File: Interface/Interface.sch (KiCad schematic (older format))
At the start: 5 parts, among them U1 PC123

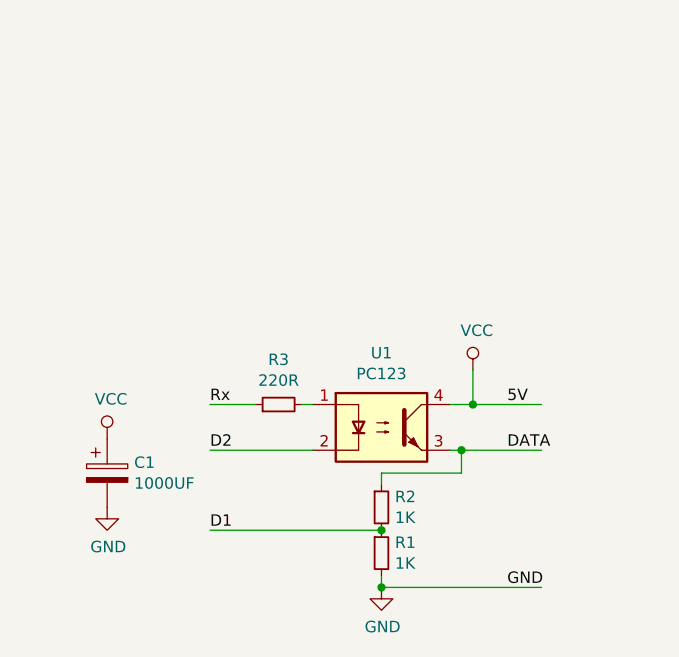
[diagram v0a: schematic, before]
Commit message: Updated interface schematic
Updated interface schematic, now using 1 bit bus transceiver
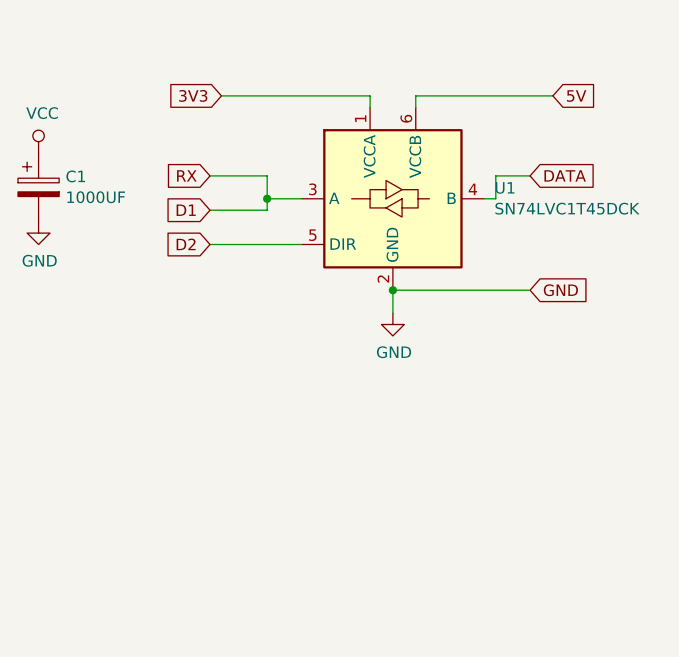
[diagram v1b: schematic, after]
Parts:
- removed R1, R2: 1K, symbol Device:R_Small
- removed R3: 220R, symbol Device:R_Small
- removed U1: PC123, Package_DIP:DIP-4_W7.62mm, symbol Isolator:PC817
- added U1: SN74LVC1T45DCK, Package_TO_SOT_SMD:SOT-363_SC-70-6, symbol Logic_LevelTranslator:SN74LVC1T45DCK
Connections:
- net labels added: 3V3, RX
- net labels removed: Rx
- wire segments 14 -> 15
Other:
- moved on the sheet: C1
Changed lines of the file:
@@
 EESchema Schematic File Version 4
+LIBS:Interface-cache
 EELAYER 30 0
 EELAYER END
@@
 $EndDescr
 $Comp
-L Isolator:PC817 U1
-U 1 1 5D6EC97C
-P 5150 2950
-F 0 "U1" H 5150 3275 50  0000 C CNN
-F 1 "PC123" H 5150 3184 50  0000 C CNN
-F 2 "Package_DIP:DIP-4_W7.62mm" H 4950 2750 50  0001 L CIN
-F 3 "http://www.soselectronic.cz/a_info/resource/d/pc817.pdf" H 5150 2950 50  0001 L CNN
-	1    5150 2950
+L power:VCC #PWR?
+U 1 1 5D70837B
+P 3650 1750
+F 0 "#PWR?" H 3650 1600 50  0001 C CNN
+F 1 "VCC" H 3667 1923 50  0000 C CNN
+F 2 "" H 3650 1750 50  0001 C CNN
+F 3 "" H 3650 1750 50  0001 C CNN
+	1    3650 1750
+	1    0    0    -1
+$EndComp
+$Comp
+L Logic_LevelTranslator:SN74LVC1T45DCK U1
+U 1 1 5E9CDB6D
+P 5200 1950
+F 0 "U1" H 5644 1996 50  0000 L CNN
+F 1 "SN74LVC1T45DCK" H 5644 1905 50  0000 L CNN
+F 2 "Package_TO_SOT_SMD:SOT-363_SC-70-6" H 5200 1500 50  0001 C CNN
+F 3 "http://www.ti.com/lit/ds/symlink/sn74lvc1t45.pdf" H 4300 1300 50  0001 C CNN
+	1    5200 1950
 	1    0    0    -1
 $EndComp
 Wire Wire Line
-	4800 2850 4850 2850
+	4400 2150 4800 2150
 Wire Wire Line
-	4600 2850 4400 2850
-Text Label 4400 2850 0    50   ~ 0
-Rx
+	5300 1550 5300 1500
 Wire Wire Line
-	4850 3050 4400 3050
-Text Label 4400 3050 0    50   ~ 0
+	5100 1550 5100 1500
+Text GLabel 4400 1850 0    50   Input ~ 0
+RX
+Text GLabel 4400 2000 0    50   Input ~ 0
+D1
+Text GLabel 5800 1850 2    50   Input ~ 0
+DATA
+Text GLabel 5800 2350 2    50   Input ~ 0
+GND
+Text GLabel 5900 1500 2    50   Input ~ 0
+5V
+Text GLabel 4450 1500 0    50   Input ~ 0
+3V3
+Text GLabel 4400 2150 0    50   Input ~ 0
 D2
+Wire Wire Line
+	4650 1850 4650 1950
+Wire Wire Line
+	4650 1950 4800 1950
+Wire Wire Line
+	4650 2000 4650 1950
+Wire Wire Line
+	4400 2000 4650 2000
+Connection ~ 4650 1950
+Wire Wire Line
+	4400 1850 4650 1850
+Wire Wire Line
+	5100 1500 4450 1500
+Wire Wire Line
+	5200 2350 5800 2350
+Wire Wire Line
+	5300 1500 5900 1500
+Wire Wire Line
+	5600 1950 5650 1950
+Wire Wire Line
+	5650 1950 5650 1850
+Wire Wire Line
+	5650 1850 5800 1850
 $Comp
-L power:VCC #PWR?
-U 1 1 5D6F0E03
-P 5550 2700
-F 0 "#PWR?" H 5550 2550 50  0001 C CNN
-F 1 "VCC" H 5567 2873 50  0000 C CNN
-F 2 "" H 5550 2700 50  0001 C CNN
-F 3 "" H 5550 2700 50  0001 C CNN
-	1    5550 2700
-	1    0    0    -1
-$EndComp
-Wire Wire Line
-	5450 3050 5500 3050
-Text Label 5700 3050 0    50   ~ 0
-DATA
-Text Label 4400 3400 0    50   ~ 0
-D1
-$Comp
-L power:GND #PWR?
-U 1 1 5D6F335B
-P 5150 3650
-F 0 "#PWR?" H 5150 3400 50  0001 C CNN
-F 1 "GND" H 5155 3477 50  0000 C CNN
-F 2 "" H 5150 3650 50  0001 C CNN
-F 3 "" H 5150 3650 50  0001 C CNN
-	1    5150 3650
-	1    0    0    -1
-$EndComp
-Wire Wire Line
-	5450 2850 5550 2850
-Wire Wire Line
-	5550 2700 5550 2850
-Connection ~ 5550 2850
-Wire Wire Line
-	5550 2850 5850 2850
-$Comp
-L Device:R_Small R2
-U 1 1 5D6F2079
-P 5150 3300
-F 0 "R2" H 5209 3346 50  0000 L CNN
-F 1 "1K" H 5209 3255 50  0000 L CNN
-F 2 "" H 5150 3300 50  0001 C CNN
-F 3 "~" H 5150 3300 50  0001 C CNN
-	1    5150 3300
-	1    0    0    -1
-$EndComp
-$Comp
-L Device:R_Small R3
-U 1 1 5D6EE00F
-P 4700 2850
-F 0 "R3" V 4896 2850 50  0000 C CNN
-F 1 "220R" V 4805 2850 50  0000 C CNN
-F 2 "" H 4700 2850 50  0001 C CNN
-F 3 "~" H 4700 2850 50  0001 C CNN
-	1    4700 2850
-	0    -1   -1   0
-$EndComp
-Text Label 5700 2850 0    50   ~ 0
-5V
-$Comp
-L Device:R_Small R1
-U 1 1 5D6F23A8
-P 5150 3500
-F 0 "R1" H 5209 3546 50  0000 L CNN
-F 1 "1K" H 5209 3455 50  0000 L CNN
-F 2 "" H 5150 3500 50  0001 C CNN
-F 3 "~" H 5150 3500 50  0001 C CNN
-	1    5150 3500
-	1    0    0    -1
-$EndComp
-Connection ~ 5150 3400
-Connection ~ 5500 3050
-Wire Wire Line
-	5500 3050 5850 3050
-Wire Wire Line
-	5500 3150 5150 3150
-Wire Wire Line
-	5150 3150 5150 3200
-Wire Wire Line
-	5500 3150 5500 3050
-Wire Wire Line
-	4400 3400 5150 3400
-$Comp
-L power:VCC #PWR?
-U 1 1 5D70837B
-P 3950 3000
-F 0 "#PWR?" H 3950 2850 50  0001 C CNN
-F 1 "VCC" H 3967 3173 50  0000 C CNN
-F 2 "" H 3950 3000 50  0001 C CNN
-F 3 "" H 3950 3000 50  0001 C CNN
-	1    3950 3000
+L Device:CP C1
+U 1 1 5D708E3A
+P 3650 1900
+F 0 "C1" H 3768 1946 50  0000 L CNN
+F 1 "1000UF" H 3768 1855 50  0000 L CNN
+F 2 "" H 3688 1750 50  0001 C CNN
+F 3 "~" H 3650 1900 50  0001 C CNN
+	1    3650 1900
 	1    0    0    -1
 $EndComp
@@
 L power:GND #PWR?
 U 1 1 5D708717
-P 3950 3300
-F 0 "#PWR?" H 3950 3050 50  0001 C CNN
-F 1 "GND" H 3955 3127 50  0000 C CNN
-F 2 "" H 3950 3300 50  0001 C CNN
-F 3 "" H 3950 3300 50  0001 C CNN
-	1    3950 3300
+P 3650 2050
+F 0 "#PWR?" H 3650 1800 50  0001 C CNN
+F 1 "GND" H 3655 1877 50  0000 C CNN
+F 2 "" H 3650 2050 50  0001 C CNN
+F 3 "" H 3650 2050 50  0001 C CNN
+	1    3650 2050
 	1    0    0    -1
 $EndComp
 $Comp
-L Device:CP C1
-U 1 1 5D708E3A
-P 3950 3150
-F 0 "C1" H 4068 3196 50  0000 L CNN
-F 1 "1000UF" H 4068 3105 50  0000 L CNN
-F 2 "" H 3988 3000 50  0001 C CNN
-F 3 "~" H 3950 3150 50  0001 C CNN
-	1    3950 3150
+L power:GND #PWR?
+U 1 1 5E9D72B6
+P 5200 2450
+F 0 "#PWR?" H 5200 2200 50  0001 C CNN
+F 1 "GND" H 5205 2277 50  0000 C CNN
+F 2 "" H 5200 2450 50  0001 C CNN
+F 3 "" H 5200 2450 50  0001 C CNN
+	1    5200 2450
 	1    0    0    -1
 $EndComp
 Wire Wire Line
-	5150 3650 5150 3600
-Wire Wire Line
-	5150 3650 5850 3650
-Connection ~ 5150 3650
-Text Label 5700 3650 0    50   ~ 0
-GND
+	5200 2450 5200 2350
+Connection ~ 5200 2350
 $EndSCHEMATC

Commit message: Added MQTT + tweaks
Added MQTT and parameters to config page, reworked API, tweaked interface schematic, improved test page.
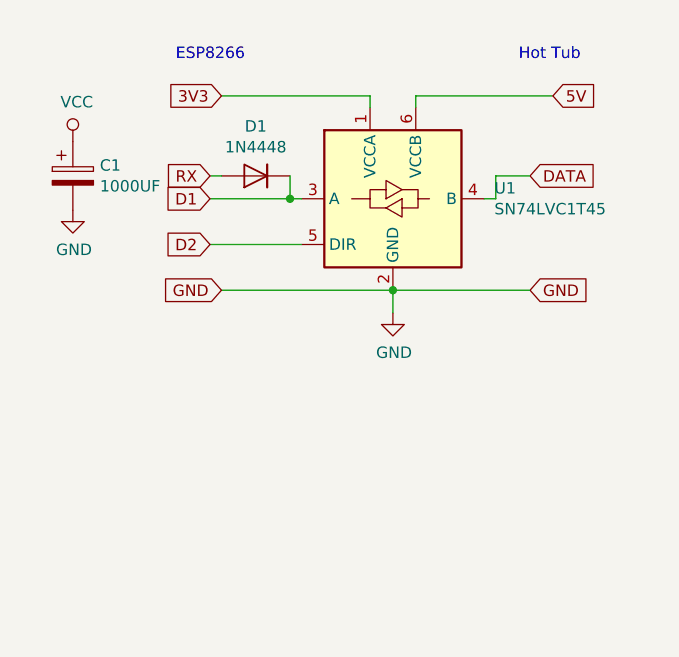
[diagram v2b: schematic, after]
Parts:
- added D1: 1N4448, Diode_SMD:D_SOD-123, symbol Diode:1N4448W
- U1: value SN74LVC1T45DCK -> SN74LVC1T45
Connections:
- net D1: now also D1.1 (K)
- new net RX: D1.2 (A)
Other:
- note added: "ESP8266"
- note added: "Hot Tub"
- moved on the sheet: C1
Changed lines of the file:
@@
 L power:VCC #PWR?
 U 1 1 5D70837B
-P 3650 1750
-F 0 "#PWR?" H 3650 1600 50  0001 C CNN
-F 1 "VCC" H 3667 1923 50  0000 C CNN
-F 2 "" H 3650 1750 50  0001 C CNN
-F 3 "" H 3650 1750 50  0001 C CNN
-	1    3650 1750
+P 3800 1700
+F 0 "#PWR?" H 3800 1550 50  0001 C CNN
+F 1 "VCC" H 3817 1873 50  0000 C CNN
+F 2 "" H 3800 1700 50  0001 C CNN
+F 3 "" H 3800 1700 50  0001 C CNN
+	1    3800 1700
 	1    0    0    -1
 $EndComp
@@
 P 5200 1950
 F 0 "U1" H 5644 1996 50  0000 L CNN
-F 1 "SN74LVC1T45DCK" H 5644 1905 50  0000 L CNN
+F 1 "SN74LVC1T45" H 5644 1905 50  0000 L CNN
 F 2 "Package_TO_SOT_SMD:SOT-363_SC-70-6" H 5200 1500 50  0001 C CNN
 F 3 "http://www.ti.com/lit/ds/symlink/sn74lvc1t45.pdf" H 4300 1300 50  0001 C CNN
@@
 Text GLabel 4400 1850 0    50   Input ~ 0
 RX
-Text GLabel 4400 2000 0    50   Input ~ 0
+Text GLabel 4400 1950 0    50   Input ~ 0
 D1
 Text GLabel 5800 1850 2    50   Input ~ 0
@@
 Text GLabel 5800 2350 2    50   Input ~ 0
 GND
-Text GLabel 5900 1500 2    50   Input ~ 0
-5V
 Text GLabel 4450 1500 0    50   Input ~ 0
 3V3
@@
 D2
 Wire Wire Line
-	4650 1850 4650 1950
-Wire Wire Line
-	4650 1950 4800 1950
-Wire Wire Line
-	4650 2000 4650 1950
-Wire Wire Line
-	4400 2000 4650 2000
-Connection ~ 4650 1950
-Wire Wire Line
-	4400 1850 4650 1850
-Wire Wire Line
 	5100 1500 4450 1500
 Wire Wire Line
 	5200 2350 5800 2350
-Wire Wire Line
-	5300 1500 5900 1500
 Wire Wire Line
 	5600 1950 5650 1950
@@
 L Device:CP C1
 U 1 1 5D708E3A
-P 3650 1900
-F 0 "C1" H 3768 1946 50  0000 L CNN
-F 1 "1000UF" H 3768 1855 50  0000 L CNN
-F 2 "" H 3688 1750 50  0001 C CNN
-F 3 "~" H 3650 1900 50  0001 C CNN
-	1    3650 1900
+P 3800 1850
+F 0 "C1" H 3918 1896 50  0000 L CNN
+F 1 "1000UF" H 3918 1805 50  0000 L CNN
+F 2 "" H 3838 1700 50  0001 C CNN
+F 3 "~" H 3800 1850 50  0001 C CNN
+	1    3800 1850
 	1    0    0    -1
 $EndComp
@@
 L power:GND #PWR?
 U 1 1 5D708717
-P 3650 2050
-F 0 "#PWR?" H 3650 1800 50  0001 C CNN
-F 1 "GND" H 3655 1877 50  0000 C CNN
-F 2 "" H 3650 2050 50  0001 C CNN
-F 3 "" H 3650 2050 50  0001 C CNN
-	1    3650 2050
+P 3800 2000
+F 0 "#PWR?" H 3800 1750 50  0001 C CNN
+F 1 "GND" H 3805 1827 50  0000 C CNN
+F 2 "" H 3800 2000 50  0001 C CNN
+F 3 "" H 3800 2000 50  0001 C CNN
+	1    3800 2000
 	1    0    0    -1
 $EndComp
@@
 	5200 2450 5200 2350
 Connection ~ 5200 2350
+$Comp
+L Diode:1N4448W D1
+U 1 1 5EA5CF14
+P 4600 1850
+F 0 "D1" H 4600 1633 50  0000 C CNN
+F 1 "1N4448" H 4600 1724 50  0000 C CNN
+F 2 "Diode_SMD:D_SOD-123" H 4600 1675 50  0001 C CNN
+F 3 "https://www.vishay.com/docs/85722/1n4448w.pdf" H 4600 1850 50  0001 C CNN
+	1    4600 1850
+	-1   0    0    1
+$EndComp
+Wire Wire Line
+	4750 1850 4750 1950
+Wire Wire Line
+	4750 1950 4800 1950
+Wire Wire Line
+	4400 1950 4750 1950
+Connection ~ 4750 1950
+Wire Wire Line
+	4450 1850 4400 1850
+Wire Wire Line
+	5300 1500 5900 1500
+Text GLabel 5900 1500 2    50   Input ~ 0
+5V
+Text GLabel 4450 2350 0    50   Input ~ 0
+GND
+Wire Wire Line
+	4450 2350 5200 2350
+Text Notes 4250 1350 0    50   ~ 0
+ESP8266
+Text Notes 5750 1350 0    50   ~ 0
+Hot Tub
 $EndSCHEMATC

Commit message: Various refactoring
Replaced Serial logging with syslog in numerous places, disable interrupts when sending commands (attemp to reduce exceptions), fixed picking up error codes.
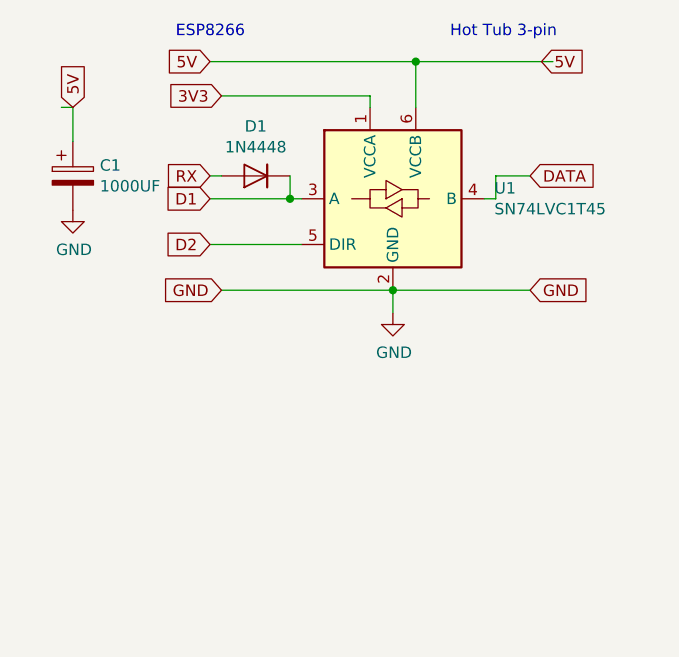
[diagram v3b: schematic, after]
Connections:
- net labels removed: VCC
- wire segments 15 -> 18
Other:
- note added: "Hot Tub 3-pin"
- note removed: "Hot Tub"
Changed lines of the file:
@@
 $EndDescr
-$Comp
-L power:VCC #PWR?
-U 1 1 5D70837B
-P 3800 1700
-F 0 "#PWR?" H 3800 1550 50  0001 C CNN
-F 1 "VCC" H 3817 1873 50  0000 C CNN
-F 2 "" H 3800 1700 50  0001 C CNN
-F 3 "" H 3800 1700 50  0001 C CNN
-	1    3800 1700
-	1    0    0    -1
-$EndComp
 $Comp
 L Logic_LevelTranslator:SN74LVC1T45DCK U1
@@
 Wire Wire Line
 	4400 2150 4800 2150
-Wire Wire Line
-	5300 1550 5300 1500
 Wire Wire Line
 	5100 1550 5100 1500
@@
 $Comp
 L power:GND #PWR?
-U 1 1 5D708717
-P 3800 2000
-F 0 "#PWR?" H 3800 1750 50  0001 C CNN
-F 1 "GND" H 3805 1827 50  0000 C CNN
-F 2 "" H 3800 2000 50  0001 C CNN
-F 3 "" H 3800 2000 50  0001 C CNN
-	1    3800 2000
-	1    0    0    -1
-$EndComp
-$Comp
-L power:GND #PWR?
 U 1 1 5E9D72B6
 P 5200 2450
@@
 Wire Wire Line
 	4450 1850 4400 1850
-Wire Wire Line
-	5300 1500 5900 1500
-Text GLabel 5900 1500 2    50   Input ~ 0
+Text GLabel 5850 1350 2    50   Input ~ 0
 5V
 Text GLabel 4450 2350 0    50   Input ~ 0
@@
 Wire Wire Line
 	4450 2350 5200 2350
-Text Notes 4250 1350 0    50   ~ 0
+Text Notes 4250 1250 0    50   ~ 0
 ESP8266
-Text Notes 5750 1350 0    50   ~ 0
-Hot Tub
+Text Notes 5450 1250 0    50   ~ 0
+Hot Tub 3-pin
+Text GLabel 4400 1350 0    50   Input ~ 0
+5V
+Wire Wire Line
+	4400 1350 5300 1350
+Connection ~ 5300 1350
+Wire Wire Line
+	5300 1350 5900 1350
+Wire Wire Line
+	5300 1350 5300 1550
+$Comp
+L power:GND #PWR?
+U 1 1 5D708717
+P 3800 2000
+F 0 "#PWR?" H 3800 1750 50  0001 C CNN
+F 1 "GND" H 3805 1827 50  0000 C CNN
+F 2 "" H 3800 2000 50  0001 C CNN
+F 3 "" H 3800 2000 50  0001 C CNN
+	1    3800 2000
+	1    0    0    -1
+$EndComp
+Text GLabel 3800 1550 1    50   Input ~ 0
+5V
+Wire Wire Line
+	3750 1550 3800 1550
+Wire Wire Line
+	3800 1550 3800 1700
 $EndSCHEMATC
